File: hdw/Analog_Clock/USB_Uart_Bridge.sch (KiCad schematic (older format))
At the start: 39 parts, among them J1301 USB_B_Mini, U1301 TLV6700, U1302 FT234XD, U1303 74LVC1G17, U1304 TXB0102DCU, U1305 TPD3S014DBVR

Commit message: More PCB arrangement
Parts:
- removed C1305, C1306, C1310, C1312, C1313: 0.1uF, Capacitors_SMD:C_0603, symbol Custom_Library:C_Custom
- removed C1308: 10uF, Capacitors_SMD:C_0603, symbol Custom_Library:C_Custom
- removed L1301: 600R 0.5A, Inductors_SMD:L_0603, symbol Device:Ferrite_Bead
- removed R1306, R1308: 100k, Resistors_SMD:R_0603, symbol Custom_Library:R_Custom
- removed R1307: 1k, Resistors_SMD:R_0603, symbol Custom_Library:R_Custom
- removed R1309, R1313: 10, Resistors_SMD:R_0603, symbol Custom_Library:R_Custom
- removed R1310: 0.02, Resistors_SMD:R_0612, symbol Custom_Library:R_Custom
- removed TP1301: TP, Custom Footprints Library:Test_Point, symbol Custom_Library:TP
- removed U1301: TLV6700, Package_TO_SOT_SMD:SOT-23-6, symbol Custom_Library:TLV6700
- removed U1303: 74LVC1G17, TO_SOT_Packages_SMD:SOT-353_SC-70-5, symbol Custom_Library:74LVC1G17_Power
- removed U1304: TXB0102DCU, Package_SO:VSSOP-8_2.4x2.1mm_P0.5mm, symbol Logic_LevelTranslator:TXB0102DCU
- removed U1305: TPD3S014DBVR, TO_SOT_Packages_SMD:SOT-23-6, symbol Custom_Library:TPD3S014DBVR
- added U1301: TPD2EUSB30A, Package_TO_SOT_SMD:Texas_DRT-3, symbol Power_Protection:TPD2EUSB30A
- added U1303: TLV6700, Package_TO_SOT_SMD:SOT-23-6, symbol Custom_Library:TLV6700
- C1303: footprint Capacitors_SMD:C_0805 -> Capacitors_SMD:C_0603; Digi-Key PN 490-18664-1-ND -> 490-10474-1-ND; Voltage 50V -> 10V; display_footprint 0805 -> 0603
- R1302: Digi-Key PN 311-487KHRCT-ND -> (none)
- R1303: Digi-Key PN RMCF0603FT6K04CT-ND -> (none)
- R1304: Digi-Key PN RMCF0603FT40K2CT-ND -> (none)
- R1314, R1315: value 100k -> 10k; Digi-Key PN RMCF0603FT100KCT-ND -> YAG2321CT-ND
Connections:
- net +3.3V_USB is gone; now on net +3V3: C1301.1, C1307.1, R1314.1, R1315.1, U1302.3 (3V3OUT), U1302.9 (VCCIO)
- net +3V3: now also C1302.1, C1303.1, R1301.1, R1305.2, U1302.4 (VCC), U1303.5 (Vs); no longer R1305.1
- net +5V_USB: no longer C1302.1, C1303.1, R1301.1, U1302.4 (VCC)
- net CONN_USB+: now also U1301.1 (D+)
- net CONN_USB-: now also U1301.2 (D-)
- net GND: now also U1301.3 (GND), U1303.2 (GND)
- net POS5_USB_PGOOD: now also R1305.1, U1303.1 (OUTA), U1303.6 (OUTB); no longer R1305.2
- net USB_UART_RX: now also R1314.2, U1302.7 (TXD)
- net USB_UART_TX: now also R1315.2, U1302.10 (RXD)
- net at R1302.2, R1303.1: now also U1303.3 (+INA)
- net at R1303.2, R1304.1: now also U1303.4 (-INB)
- removed net USB_UART_RX_BUF: R1315.2, U1302.7 (TXD)
- removed net USB_UART_TX_BUF: R1314.2, U1302.10 (RXD)
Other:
- note added: "VCC"
- note added: "VCCIO"
- moved on the sheet: C1301, C1302, C1307, C1309, C1311, D1301, J1301, L1302, R1301, R1311, R1312, U1302

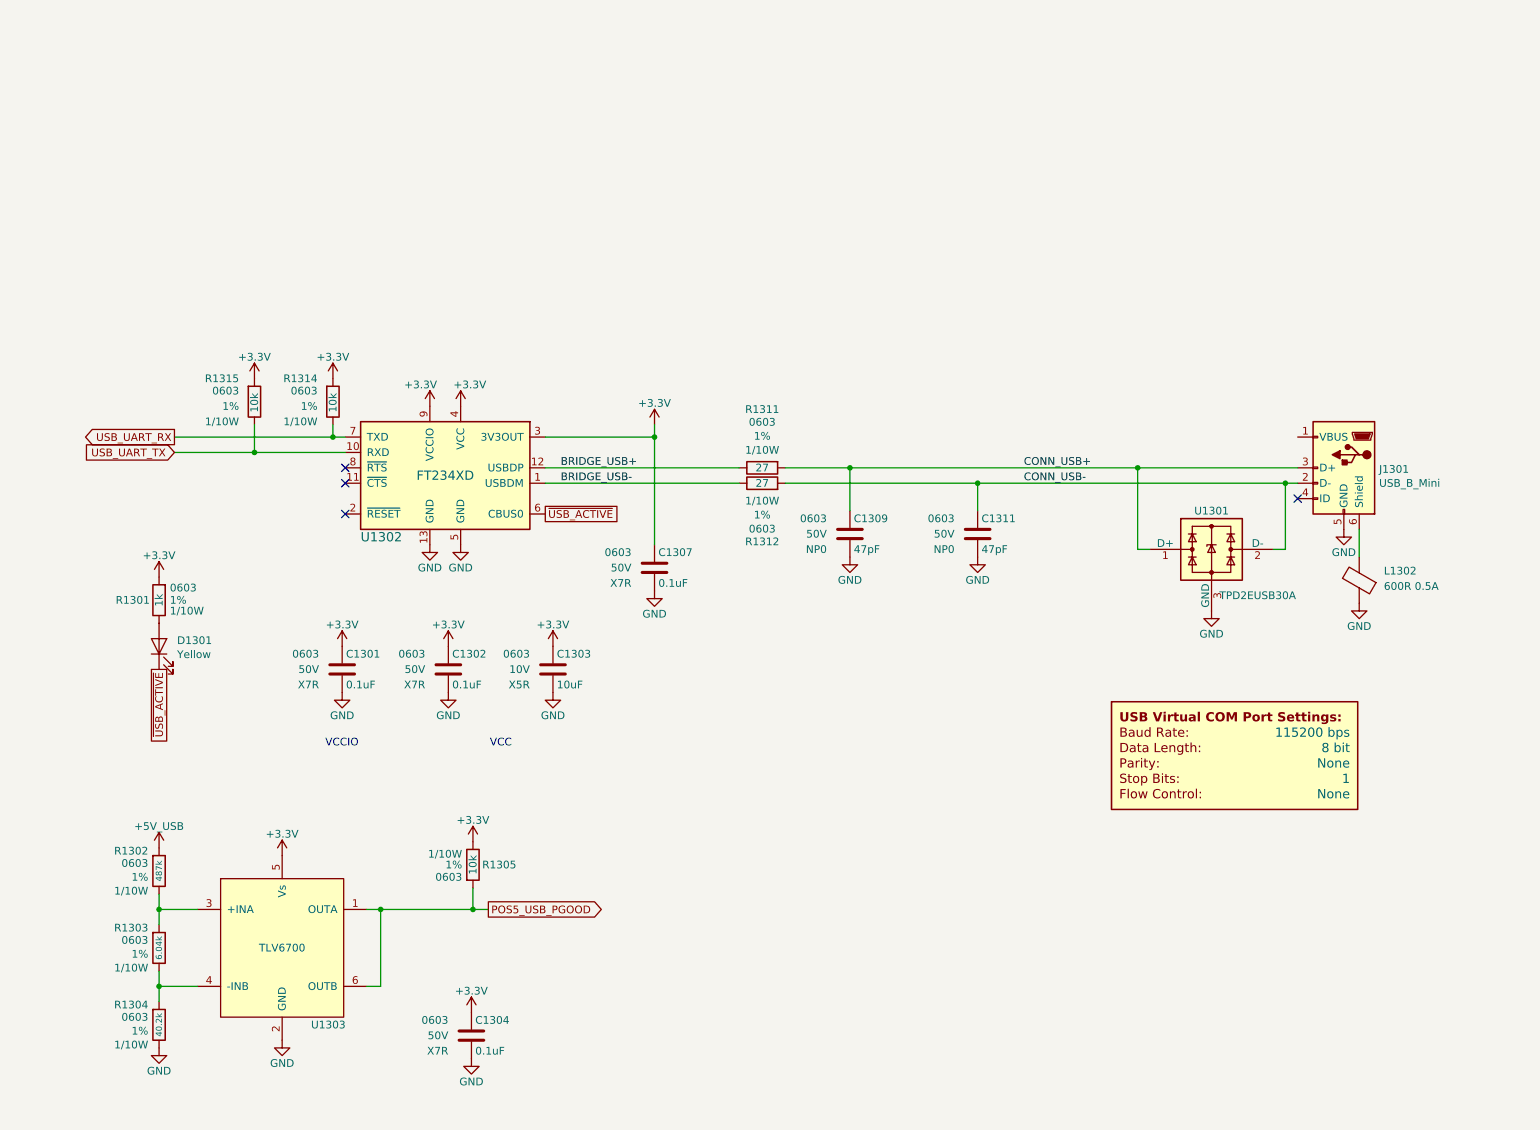
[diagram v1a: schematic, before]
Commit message: Major USB restructuring
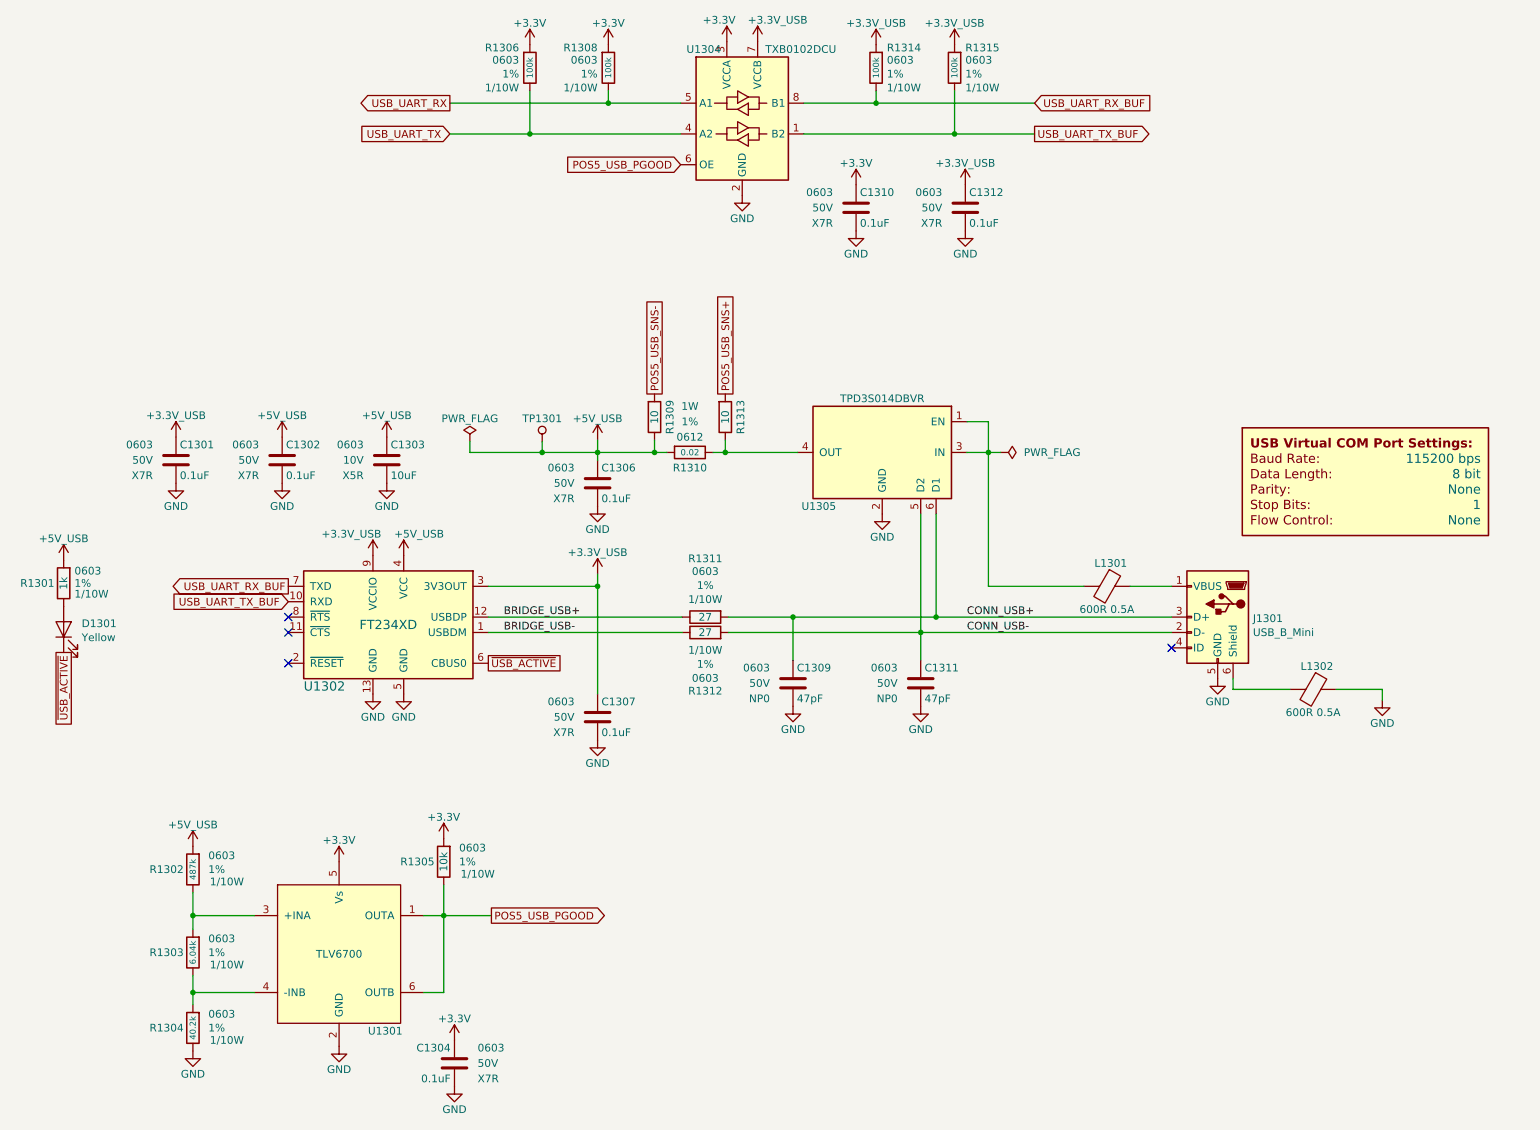
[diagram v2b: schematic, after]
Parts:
- removed U1301: TPD2EUSB30A, Package_TO_SOT_SMD:Texas_DRT-3, symbol Power_Protection:TPD2EUSB30A
- removed U1303: TLV6700, Package_TO_SOT_SMD:SOT-23-6, symbol Custom_Library:TLV6700
- added C1306, C1310, C1312: 0.1uF, Capacitors_SMD:C_0603, symbol Custom_Library:C_Custom
- added L1301: 600R 0.5A, Inductors_SMD:L_0603, symbol Device:Ferrite_Bead
- added R1306, R1308: 100k, Resistors_SMD:R_0603, symbol Custom_Library:R_Custom
- added R1309, R1313: 10, Resistors_SMD:R_0603, symbol Custom_Library:R_Custom
- added R1310: 0.02, Resistors_SMD:R_0612, symbol Custom_Library:R_Custom
- added TP1301: TP, Custom Footprints Library:Test_Point, symbol Custom_Library:TP
- added U1301: TLV6700, Package_TO_SOT_SMD:SOT-23-6, symbol Custom_Library:TLV6700
- added U1304: TXB0102DCU, Package_SO:VSSOP-8_2.4x2.1mm_P0.5mm, symbol Logic_LevelTranslator:TXB0102DCU
- added U1305: TPD3S014DBVR, TO_SOT_Packages_SMD:SOT-23-6, symbol Custom_Library:TPD3S014DBVR
- R1302: Digi-Key PN (none) -> 311-487KHRCT-ND
- R1303: Digi-Key PN (none) -> RMCF0603FT6K04CT-ND
- R1304: Digi-Key PN (none) -> RMCF0603FT40K2CT-ND
- R1314, R1315: value 10k -> 100k; Digi-Key PN YAG2321CT-ND -> RMCF0603FT100KCT-ND
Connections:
- net +3V3: now also R1305.1, C1310.1, R1306.1, R1308.1, U1301.5 (Vs), U1304.3 (VCCA); no longer C1301.1, C1302.1, C1303.1, C1307.1, R1301.1, R1305.2, R1314.1, R1315.1, U1302.3 (3V3OUT), U1302.4 (VCC), U1302.9 (VCCIO)
- net +5V_USB: now also C1302.1, C1303.1, R1301.1, U1302.4 (VCC), C1306.1, R1309.2, R1310.1, TP1301.1 (TP)
- net CONN_USB+: now also U1305.6 (D1)
- net CONN_USB-: now also U1305.5 (D2)
- net GND: now also C1306.2, C1310.2, C1312.2, U1301.2 (GND), U1304.2 (GND), U1305.2 (GND)
- net POS5_USB_PGOOD: now also R1305.2, U1301.1 (OUTA), U1301.6 (OUTB), U1304.6 (OE); no longer R1305.1
- net USB_UART_RX: now also R1308.2, U1304.5 (A1); no longer R1314.2, U1302.7 (TXD)
- net USB_UART_TX: now also R1306.2, U1304.4 (A2); no longer R1315.2, U1302.10 (RXD)
- net at J1301.1 (VBUS): now also L1301.1
- net at R1302.2, R1303.1: now also U1301.3 (+INA)
- net at R1303.2, R1304.1: now also U1301.4 (-INB)
- new net: L1301.2, U1305.1 (EN), U1305.3 (IN)
- new net: R1310.2, R1313.2, U1305.4 (OUT)
- new net +3.3V_USB: C1301.1, C1307.1, C1312.1, R1314.1, R1315.1, U1302.3 (3V3OUT), U1302.9 (VCCIO), U1304.7 (VCCB)
- new net POS5_USB_SNS+: R1313.1
- new net POS5_USB_SNS-: R1309.1
- new net USB_UART_RX_BUF: R1314.2, U1302.7 (TXD), U1304.8 (B1)
- new net USB_UART_TX_BUF: R1315.2, U1302.10 (RXD), U1304.1 (B2)
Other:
- note removed: "VCC"
- note removed: "VCCIO"
- moved on the sheet: C1301, C1302, C1307, C1309, C1311, D1301, J1301, L1302, R1301, R1311, R1312, U1302
